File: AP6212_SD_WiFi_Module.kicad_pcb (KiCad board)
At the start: 2 copper layers, 24.6 x 23 mm, 22 parts, among them J1 Conn_Coaxial, J2 TF_Card, U1 AP6212, Y1 26MHz

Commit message: feat: Replace 4.7uH inductor package to VLS252012
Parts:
- L2: footprint Inductor_SMD:L_TDK_NLV25_2.5x2.0mm -> Custom_Libs:IND-SMD_L2.5-W2.0_VLS2520X
- moved C8 0.24 mm to (220.6, 126.6)
- moved L2 0.19 mm to (217.6, 127.4)
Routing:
- net Net-(U1-VIN_LDO_OUT): track 8.28 -> 9.14 mm

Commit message: feat: Replace 4.7uH inductor package to SWPA252012
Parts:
- L2: footprint Custom_Libs:IND-SMD_L2.5-W2.0_VLS2520X -> Custom_Libs:IND-SMD_L2.5-W2.0
- turned L2 to 180 degrees
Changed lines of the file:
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@@
     )
   )
-  (footprint "Custom_Libs:IND-SMD_L2.5-W2.0_VLS2520X" (layer "F.Cu")
-    (at 217.59 127.406)
+  (footprint "Custom_Libs:IND-SMD_L2.5-W2.0" (layer "F.Cu")
+    (at 217.59 127.406 180)
     (property "Sheetfile" "AP6212_SD_WiFi_Module.kicad_sch")
     (property "Sheetname" "")
@@
     (property "ki_keywords" "inductor choke coil reactor magnetic")
     (attr through_hole)
-    (fp_text reference "L2" (at -0.736 -1.899) (layer "F.SilkS") hide
-        (effects (font (size 0.8 0.8) (thickness 0.15)) (justify left))
+    (fp_text reference "L2" (at -0.89 -1.931) (layer "F.SilkS") hide
+        (effects (font (size 1 1) (thickness 0.15)) (justify right))
     )
     (fp_text value "4.7uH" (at 0 -0.667) (layer "F.Fab") hide
-        (effects (font (size 1 1) (thickness 0.15)) (justify left))
-    )
-    (fp_line (start -0.287 -1.1) (end 0.287 -1.1)
-      (stroke (width 0.102) (type solid)) (layer "F.SilkS"))
-    (fp_line (start 0.287 1.1) (end -0.287 1.1)
-      (stroke (width 0.102) (type solid)) (layer "F.SilkS"))
-    (fp_circle (center -1.26 1.01) (end -1.23 1.01)
+        (effects (font (size 1 1) (thickness 0.15)) (justify right))
+    )
+    (fp_line (start -0.197 1.016) (end 0.197 1.016)
+      (stroke (width 0.254) (type solid)) (layer "F.SilkS"))
+    (fp_line (start 0.197 -1.016) (end -0.197 -1.016)
+      (stroke (width 0.254) (type solid)) (layer "F.SilkS"))
+    (fp_circle (center -1.22 0.97) (end -1.19 0.97)
       (stroke (width 0.06) (type solid)) (fill none) (layer "Eco2.User"))
     (fp_poly
       (pts
-        (xy -0.42 1)
-        (xy -1.26 0.61)
-        (xy -1.26 -0.61)
-        (xy -0.41 -1.01)
+        (xy -1.25 -1)
+        (xy -0.45 -1)
+        (xy -0.45 1)
+        (xy -1.25 1)
       )
       (stroke (width 0.12) (type solid)) (fill solid) (layer "Eco2.User"))
     (fp_poly
       (pts
-        (xy 0.41 1)
-        (xy 1.25 0.61)
-        (xy 1.25 -0.61)
-        (xy 0.4 -1.01)
+        (xy 0.45 -1)
+        (xy 1.25 -1)
+        (xy 1.25 1)
+        (xy 0.45 1)
       )
       (stroke (width 0.12) (type solid)) (fill solid) (layer "Eco2.User"))
-    (fp_line (start -1.25 -0.61) (end -1.25 0.61)
+    (fp_line (start -1.25 -1) (end 1.25 -1)
       (stroke (width 0.12) (type solid)) (layer "F.CrtYd"))
-    (fp_line (start -1.25 0.61) (end -0.41 1.01)
+    (fp_line (start -1.25 1) (end -1.25 -1)
       (stroke (width 0.12) (type solid)) (layer "F.CrtYd"))
-    (fp_line (start -0.41 1.01) (end 0.41 1.01)
+    (fp_line (start 1.25 -1) (end 1.25 1)
       (stroke (width 0.12) (type solid)) (layer "F.CrtYd"))
-    (fp_line (start -0.4 -1.01) (end -1.25 -0.61)
+    (fp_line (start 1.25 1) (end -1.25 1)
       (stroke (width 0.12) (type solid)) (layer "F.CrtYd"))
-    (fp_line (start 0.4 -1.01) (end -0.4 -1.01)
-      (stroke (width 0.12) (type solid)) (layer "F.CrtYd"))
-    (fp_line (start 0.41 1.01) (end 1.25 0.61)
-      (stroke (width 0.12) (type solid)) (layer "F.CrtYd"))
-    (fp_line (start 1.25 -0.61) (end 0.4 -1.01)
-      (stroke (width 0.12) (type solid)) (layer "F.CrtYd"))
-    (fp_line (start 1.25 0.61) (end 1.25 -0.61)
-      (stroke (width 0.12) (type solid)) (layer "F.CrtYd"))
-    (pad "1" smd rect (at -0.83 0) (size 1 2.2) (layers "F.Cu" "F.Paste" "F.Mask")
+    (pad "1" smd rect (at 1.028 0 180) (size 1.2 2.2) (layers "F.Cu" "F.Paste" "F.Mask")
       (net 12 "Net-(U1-VIN_LDO_OUT)") (pinfunction "1") (pintype "passive"))
-    (pad "2" smd rect (at 0.83 0) (size 1 2.2) (layers "F.Cu" "F.Paste" "F.Mask")
+    (pad "2" smd rect (at -1.028 0 180) (size 1.2 2.2) (layers "F.Cu" "F.Paste" "F.Mask")
       (net 13 "Net-(U1-VIN_LDO)") (pinfunction "2") (pintype "passive"))
-    (model "${KIPRJMOD}/kicad_lceda.3dshapes/IND-SMD_L2.5-W2.0-H1.2_VLS2520X.step"
-      (offset (xyz 0 0 0))
+    (model "${KIPRJMOD}/kicad_lceda.3dshapes/IND-SMD_L2.5-W2.0-H1.2.step"
+      (offset (xyz -914.349 685.775 0))
       (scale (xyz 1 1 1))
       (rotate (xyz 0 0 0))
     )
-    (model "${KIPRJMOD}/kicad_lceda.3dshapes/IND-SMD_L2.5-W2.0-H1.2_VLS2520X.wrl"
-      (offset (xyz 0 0 0))
+    (model "${KIPRJMOD}/kicad_lceda.3dshapes/IND-SMD_L2.5-W2.0-H1.2.wrl"
+      (offset (xyz -914.349 685.775 0))
       (scale (xyz 1 1 1))
       (rotate (xyz 0 0 0))
@@
   (arc (start 202.5 114.43) (mid 202.734315 114.995685) (end 203.3 115.23) (width 0.7) (layer "F.Cu") (net 11))
   (arc (start 202.5 110.15) (mid 202.734315 109.584315) (end 203.3 109.35) (width 0.7) (layer "F.Cu") (net 11))
-  (segment (start 216.76 127.406) (end 216.76 129.105) (width 0.4) (layer "F.Cu") (net 12))
   (segment (start 215.94 124.5175) (end 215.94 123.25) (width 0.4) (layer "F.Cu") (net 12))
+  (segment (start 216.562 127.406) (end 216.562 129.105) (width 0.4) (layer "F.Cu") (net 12))
   (via (at 215.94 123.25) (size 0.8) (drill 0.4) (layers "F.Cu" "B.Cu") (net 12))
-  (via (at 216.76 129.105) (size 0.8) (drill 0.4) (layers "F.Cu" "B.Cu") (net 12))
-  (segment (start 215.94 123.25) (end 215.94 128.077893) (width 0.4) (layer "B.Cu") (net 12))
-  (segment (start 216.086447 128.431447) (end 216.76 129.105) (width 0.4) (layer "B.Cu") (net 12))
-  (arc (start 216.086447 128.431447) (mid 215.97806 128.269235) (end 215.94 128.077893) (width 0.4) (layer "B.Cu") (net 12))
-  (segment (start 218.42 127.406) (end 218.42 125.2) (width 0.4) (layer "F.Cu") (net 13))
-  (segment (start 218.42 125.2) (end 218.421 125.199) (width 0.4) (layer "F.Cu") (net 13))
-  (segment (start 218.421 125.199) (end 218.0275 124.8055) (width 0.4) (layer "F.Cu") (net 13))
-  (segment (start 218.42 127.406) (end 220.551 127.406) (width 0.4) (layer "F.Cu") (net 13))
-  (segment (start 218.0275 124.8055) (end 218.0275 123.33) (width 0.4) (layer "F.Cu") (net 13))
+  (via (at 216.562 129.105) (size 0.8) (drill 0.4) (layers "F.Cu" "B.Cu") (net 12))
+  (segment (start 216.086447 128.629447) (end 216.562 129.105) (width 0.4) (layer "B.Cu") (net 12))
+  (segment (start 215.94 123.25) (end 215.94 128.275893) (width 0.4) (layer "B.Cu") (net 12))
+  (arc (start 215.94 128.275893) (mid 215.97806 128.467235) (end 216.086447 128.629447) (width 0.4) (layer "B.Cu") (net 12))
+  (segment (start 218.471553 125.209553) (end 218.173946 124.911946) (width 0.4) (layer "F.Cu") (net 13))
+  (segment (start 218.618 127.406) (end 218.618 125.563107) (width 0.4) (layer "F.Cu") (net 13))
+  (segment (start 218.0275 124.558393) (end 218.0275 123.33) (width 0.4) (layer "F.Cu") (net 13))
+  (segment (start 218.618 127.406) (end 220.551 127.406) (width 0.4) (layer "F.Cu") (net 13))
+  (arc (start 218.173946 124.911946) (mid 218.06556 124.749734) (end 218.0275 124.558393) (width 0.4) (layer "F.Cu") (net 13))
+  (arc (start 218.471553 125.209553) (mid 218.57994 125.371765) (end 218.618 125.563107) (width 0.4) (layer "F.Cu") (net 13))
   (segment (start 209.64 124.5175) (end 209.64 123.659107) (width 0.3) (layer "F.Cu") (net 14))
   (segment (start 209.183 122.995) (end 209.493554 123.305554) (width 0.3) (layer "F.Cu") (net 14))
@@
       )
     )
+  )
+  (zone (net 0) (net_name "") (layer "F.Cu") (hatch edge 0.5)
+    (connect_pads (clearance 0))
+    (min_thickness 0.25) (filled_areas_thickness no)
+    (keepout (tracks allowed) (vias allowed) (pads allowed) (copperpour not_allowed) (footprints allowed))
+    (fill (thermal_gap 0.5) (thermal_bridge_width 0.5))
+    (polygon
+      (pts
+        (xy 217.95 128.8)
+        (xy 217.28 128.8)
+        (xy 217.29 128.78)
+        (xy 217.34 128.74)
+        (xy 217.41 128.67)
+        (xy 217.45 128.58)
+        (xy 217.5 128.52)
+        (xy 217.57 128.49)
+        (xy 217.66 128.51)
+        (xy 217.72 128.56)
+        (xy 217.78 128.68)
+        (xy 217.85 128.75)
+      )
+    )

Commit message: feat: Modify the C7 parameter value of 0.1 uF
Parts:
- C7: value 100uF -> 0.1uF
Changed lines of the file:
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@@
         (effects (font (size 1 1) (thickness 0.15)))
     )
-    (fp_text value "100uF" (at 0 1.43) (layer "F.Fab") hide
+    (fp_text value "0.1uF" (at 0 1.43) (layer "F.Fab") hide
         (effects (font (size 1 1) (thickness 0.15)))
     )
@@
         (effects (font (size 1 1) (thickness 0.15)) (justify right))
     )
-    (fp_text value "4.7uH" (at 0 -0.667) (layer "F.Fab") hide
-        (effects (font (size 1 1) (thickness 0.15)) (justify right))
+    (fp_text value "4.7uH" (at 0 0) (layer "F.Fab")
+        (effects (font (size 0.8 0.8) (thickness 0.15)))
     )
     (fp_line (start -0.197 1.016) (end 0.197 1.016)

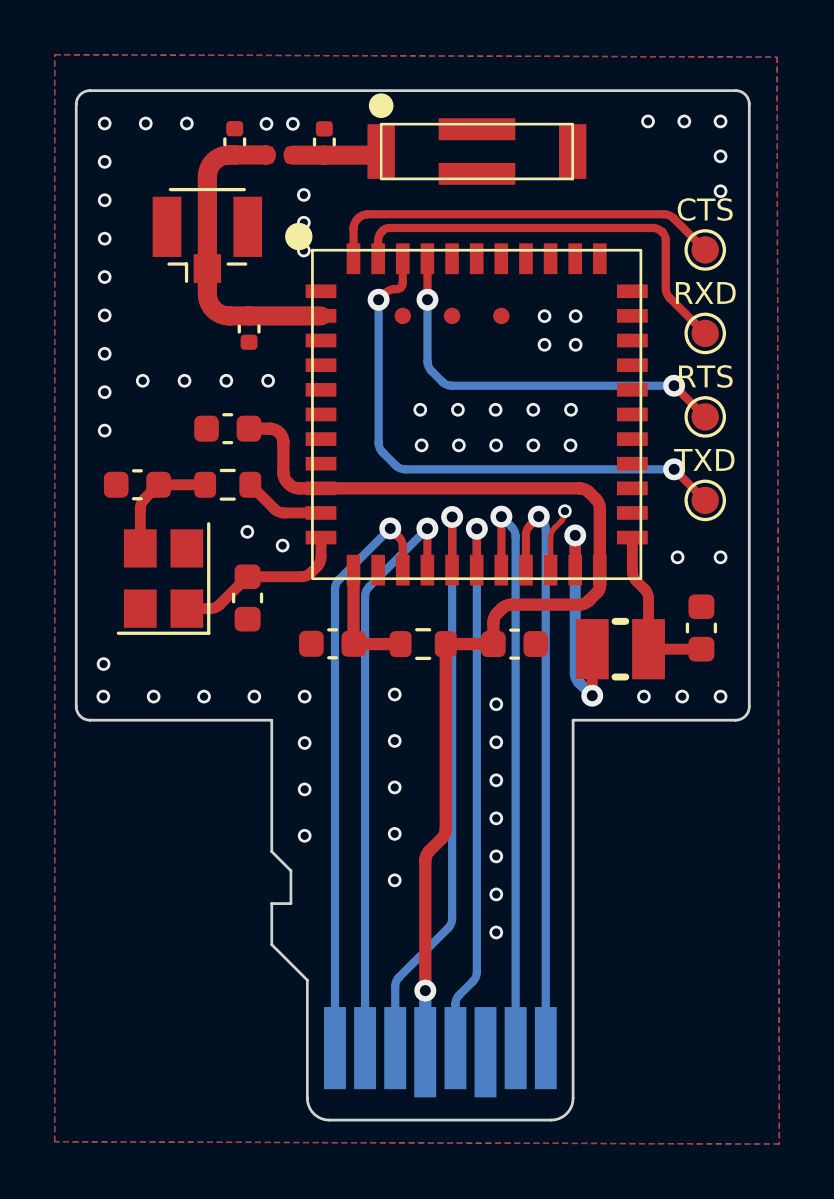
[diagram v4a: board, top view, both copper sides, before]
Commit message: feat: Removed the test point and completed the LPO part of the peripheral circuit
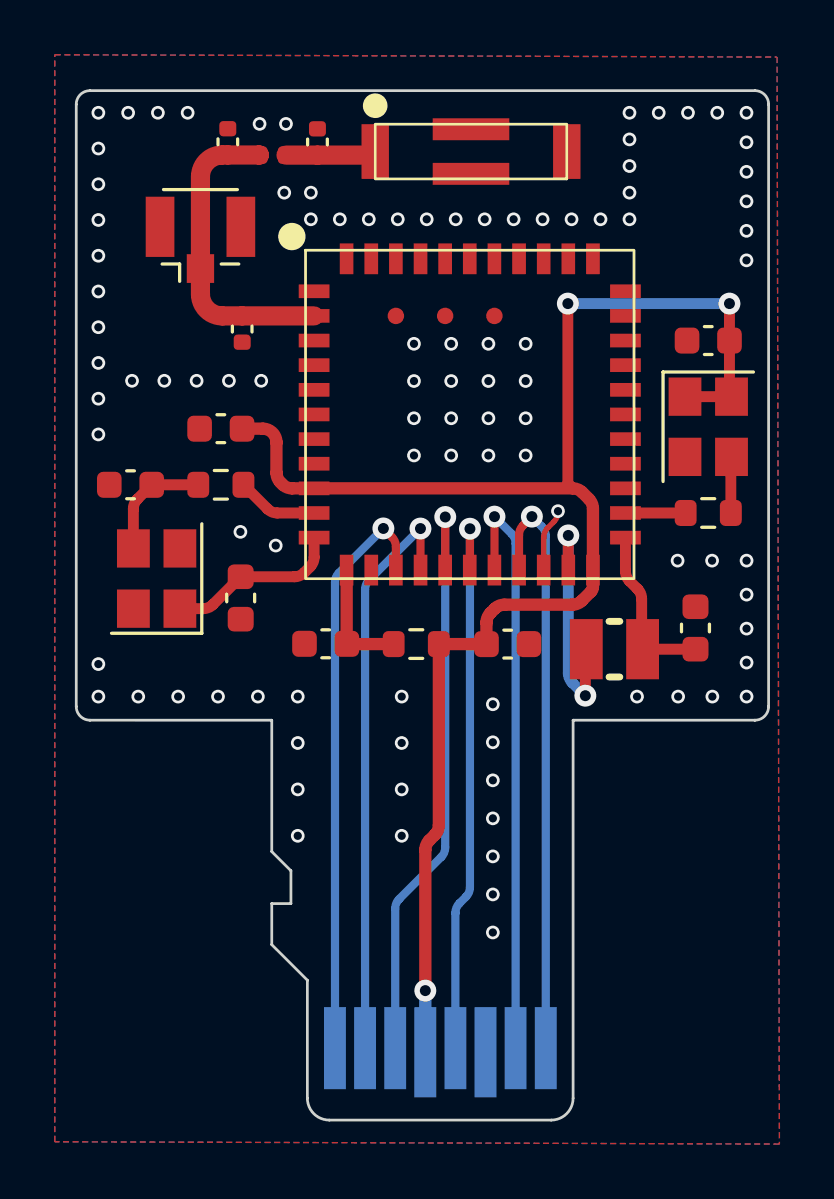
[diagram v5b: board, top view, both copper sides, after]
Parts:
- removed CTS: CTS, TestPoint:TestPoint_Pad_D1.0mm
- removed RTS: RTS, TestPoint:TestPoint_Pad_D1.0mm
- removed RXD: RXD, TestPoint:TestPoint_Pad_D1.0mm
- removed TXD: TXD, TestPoint:TestPoint_Pad_D1.0mm
- added C10: 0.1uF, Capacitor_SMD:C_0603_1608Metric, F.Cu at (220.8, 116.1)
- added R3: 1K, Resistor_SMD:R_0603_1608Metric, F.Cu at (220.8, 122.4)
- added X1: 32.768KHz, Crystal:Crystal_SMD_3225-4Pin_3.2x2.5mm, F.Cu at (220.8, 119.3)
- moved C1 0.25 mm to (199.7, 121.4)
- moved C2 0.25 mm to (203.7, 125.5)
- moved C3 0.25 mm to (206.5, 108.9)
- moved C4 0.25 mm to (203.2, 108.9)
- moved C5 0.25 mm to (203.8, 115.7)
- moved C6 0.25 mm to (203.0, 119.3)
- moved C7 0.25 mm to (206.8, 127.2)
- moved C9 0.25 mm to (213.5, 127.2)
- moved J1 0.25 mm to (202.2, 112.5)
- moved L1 0.25 mm to (204.9, 109.4)
- moved R1 0.25 mm to (203.0, 121.4)
- moved R2 0.25 mm to (210.1, 127.2)
- moved U1 0.25 mm to (212.1, 118.8)
- moved Y1 0.25 mm to (200.6, 124.8)
- moved AE1 0.22 mm to (212.1, 109.2)
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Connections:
- U1 pad 24: unconnected-(U1-LPO-Pad24) -> Net-(U1-LPO)
- U1 pad 41: Net-(U1-UART_RTS_N) -> unconnected-(U1-UART_RTS_N-Pad41)
- U1 pad 42: Net-(U1-UART_TXD) -> unconnected-(U1-UART_TXD-Pad42)
- U1 pad 43: Net-(U1-UART_RXD) -> unconnected-(U1-UART_RXD-Pad43)
- U1 pad 44: Net-(U1-UART_CTS_N) -> unconnected-(U1-UART_CTS_N-Pad44)
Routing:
- net Net-(U1-UART_TXD): track 20.1 -> 0.00 mm, vias 2 -> 0
- net VCC: track 40.0 -> 57.7 mm, vias 1 -> 3
- net Net-(U1-UART_RXD): track 15.7 -> 0.00 mm
- net Net-(U1-UART_RTS_N): track 14.8 -> 0.00 mm, vias 2 -> 0
- net Net-(U1-UART_CTS_N): track 14.8 -> 0.00 mm
- net Net-(X1-OUT): track 0.00 -> 2.06 mm
- net Net-(U1-LPO): track 0.00 -> 1.95 mm
- net GND: vias 68 -> 97
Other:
- board size 24.6 x 23 mm -> 25.3 x 23 mm

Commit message: feat: Increase the length of tf card body
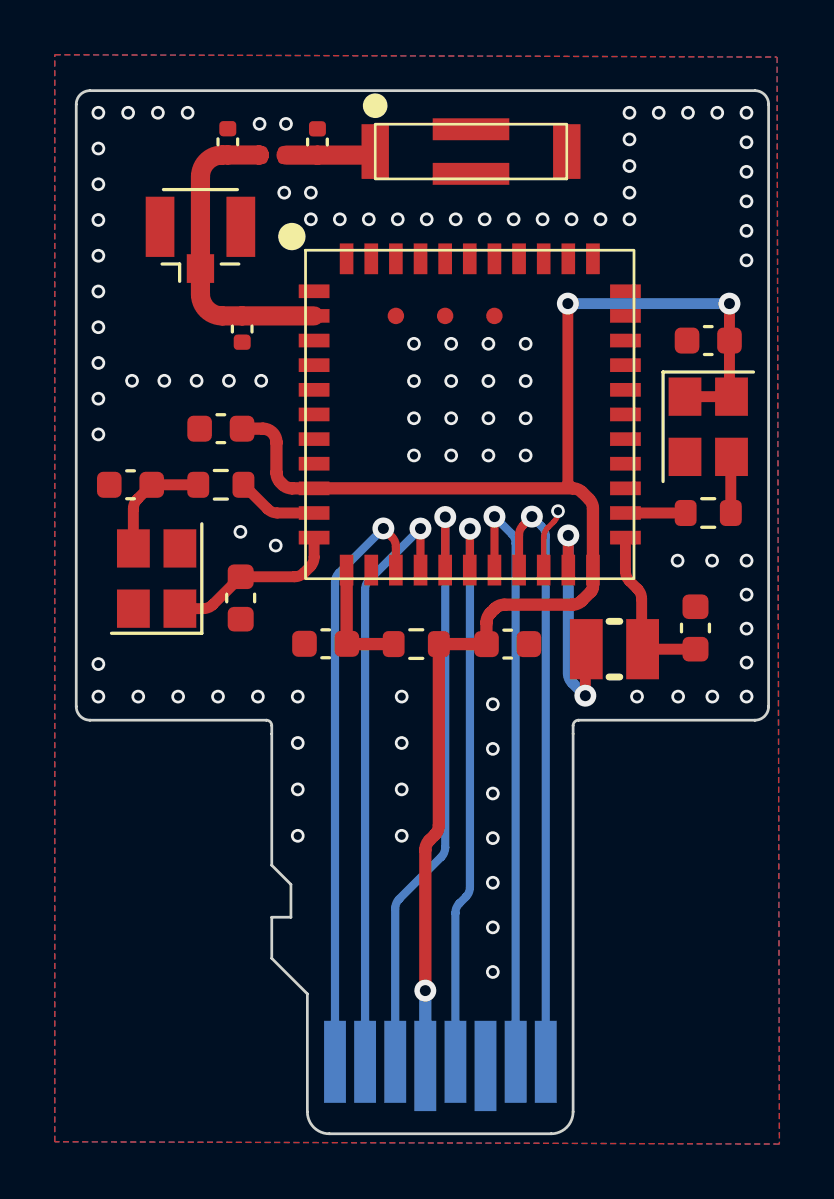
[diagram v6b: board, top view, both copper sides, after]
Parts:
- moved J2 0.50 mm to (211.0, 142.6)
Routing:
- net VCC: track 57.7 -> 58.2 mm
- net /SDIO_D3: track 21.3 -> 21.8 mm
- net /SDIO_D2: track 21.4 -> 21.9 mm
- net /SDIO_D1: track 21.7 -> 22.2 mm
- net /SDIO_D0: track 21.7 -> 22.2 mm
- net /SDIO_CMD: track 22.1 -> 22.6 mm
- net /SDIO_CLK: track 20.7 -> 21.2 mm
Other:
- board size 25.3 x 23 mm -> 25.3 x 23.5 mm

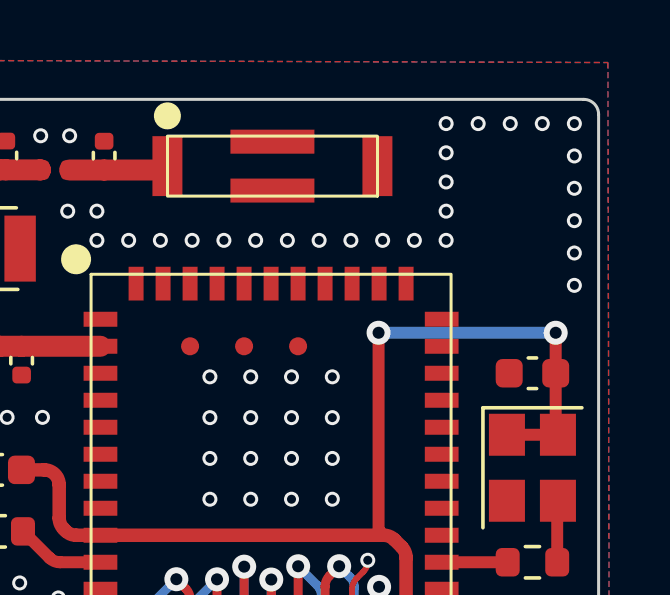
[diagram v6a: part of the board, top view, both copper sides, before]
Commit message: BT_RST_N must be driven high or low(not left floating)
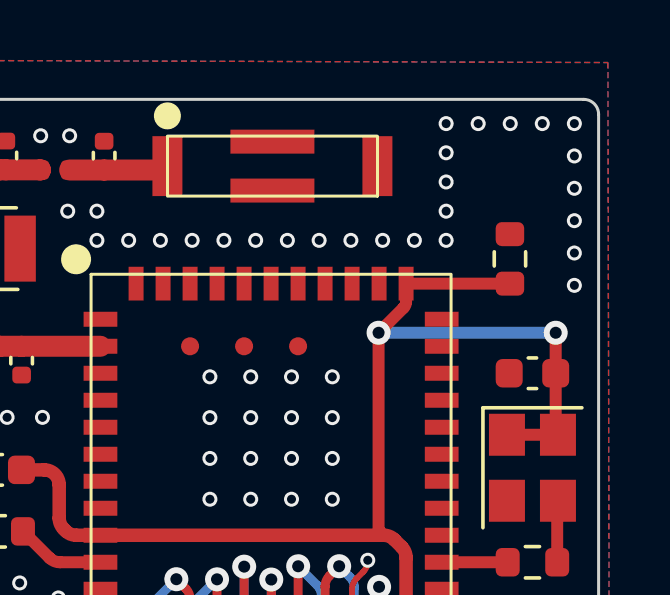
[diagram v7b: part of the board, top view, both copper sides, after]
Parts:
- added R3: 10K, Resistor_SMD:R_0603_1608Metric, F.Cu at (220.1, 112.3)
- renumbered R3 to R4
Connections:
- U1 pad 34: unconnected-(U1-BT_RST_IN-Pad34) -> VCC
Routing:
- net VCC: track 58.2 -> 63.7 mm
